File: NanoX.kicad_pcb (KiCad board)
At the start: 2 copper layers, 73.9 x 18.1 mm, 47 parts, among them J1 10118192-0001LF, J2 Conn_ARM_JTAG_SWD_10, J3 Conn_01x11, J4 NanoClassic_R, J5 Conn_01x11, J6 NanoClassic_L, SW1 SW_Push, U1 ATSAMD21G18A-AUT, U2 MCP1725-3302E_MC, U3 CAT24C16YI-GT3

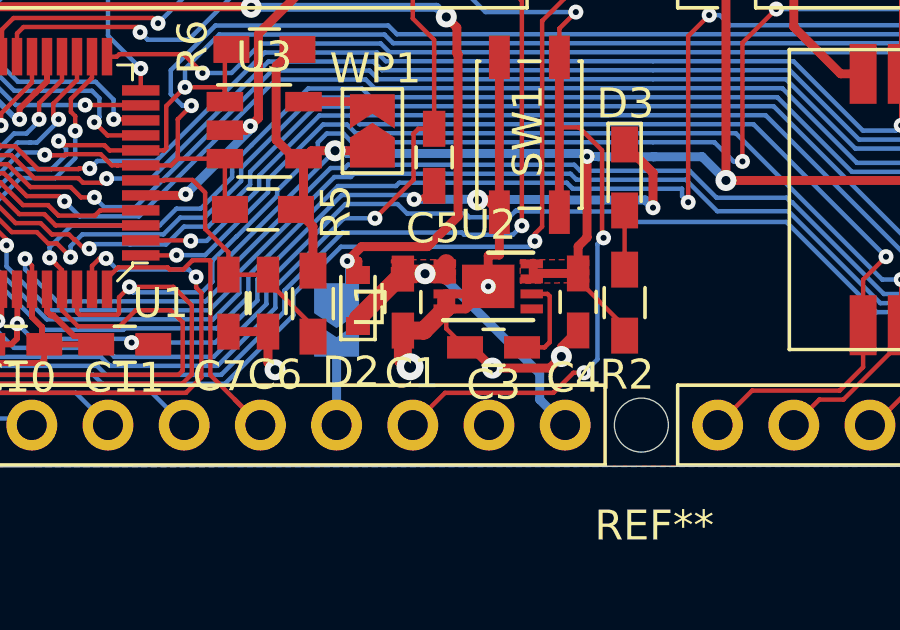
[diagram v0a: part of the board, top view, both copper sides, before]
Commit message: Change pin 3 of MCP1725 to Vin instead of GND.
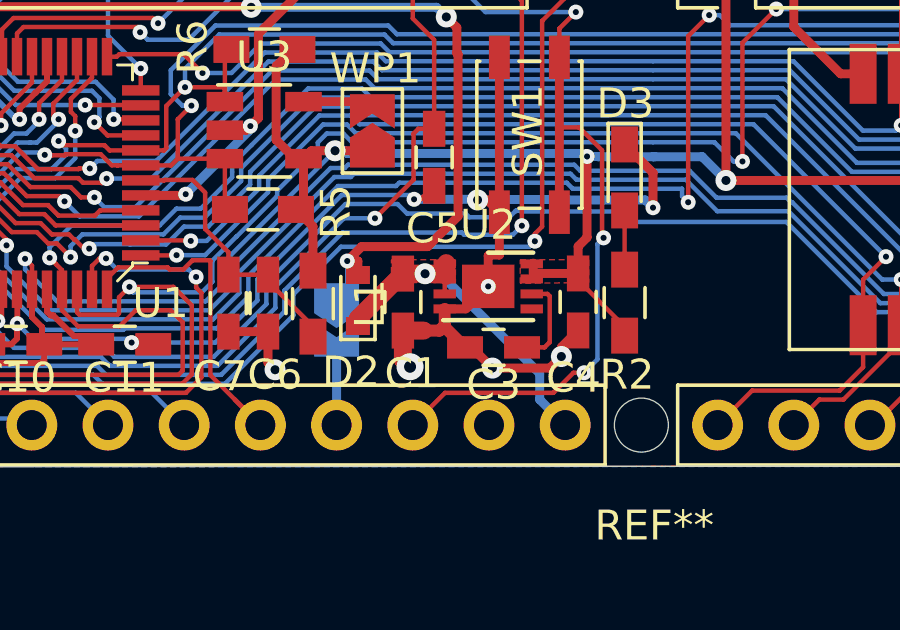
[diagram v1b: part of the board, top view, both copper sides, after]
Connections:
- U2 pad 3: GND -> VIN
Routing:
- net VIN: track 11.5 -> 12.0 mm
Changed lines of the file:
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@@
     (thickness 1.6)
     (drawings 60)
-    (tracks 1395)
+    (tracks 1398)
     (zones 0)
     (modules 47)
@@
   )
   (setup
-    (last_trace_width 0.15)
+    (last_trace_width 0.3)
     (user_trace_width 0.2)
     (user_trace_width 0.3)
@@
     (solder_mask_min_width 0.1016)
     (aux_axis_origin 0 0)
-    (visible_elements FFFFFF7F)
+    (visible_elements FFFFF77F)
     (pcbplotparams
       (layerselection 0x010f0_ffffffff)
@@
       (drillshape 0)
       (scaleselection 1)
-      (outputdirectory "Gerber-20200928/"))
+      (outputdirectory "Gerber-20201025"))
   )
   (net 0 "")
@@
       (effects (font (size 1 1) (thickness 0.15)))
     )
-    (fp_line (start 0 -1.125) (end 1.5 -1.125) (layer F.SilkS) (width 0.15))
-    (fp_line (start -1.5 1.125) (end 1.5 1.125) (layer F.SilkS) (width 0.15))
-    (fp_line (start -2.1 1.3) (end 2.1 1.3) (layer F.CrtYd) (width 0.05))
-    (fp_line (start -2.1 -1.3) (end 2.1 -1.3) (layer F.CrtYd) (width 0.05))
-    (fp_line (start 2.1 -1.3) (end 2.1 1.3) (layer F.CrtYd) (width 0.05))
-    (fp_line (start -2.1 -1.3) (end -2.1 1.3) (layer F.CrtYd) (width 0.05))
-    (fp_line (start -1.5 0) (end -0.5 -1) (layer F.Fab) (width 0.15))
-    (fp_line (start -1.5 1) (end -1.5 0) (layer F.Fab) (width 0.15))
-    (fp_line (start 1.5 1) (end -1.5 1) (layer F.Fab) (width 0.15))
-    (fp_line (start 1.5 -1) (end 1.5 1) (layer F.Fab) (width 0.15))
-    (fp_line (start -0.5 -1) (end 1.5 -1) (layer F.Fab) (width 0.15))
     (fp_text user %R (at 0 0) (layer F.Fab)
       (effects (font (size 0.7 0.7) (thickness 0.105)))
     )
-    (pad "" smd rect (at -0.4375 -0.3625) (size 0.71 0.58) (layers F.Paste))
-    (pad "" smd rect (at 0.4375 -0.3625) (size 0.71 0.58) (layers F.Paste))
-    (pad "" smd rect (at 0.4375 0.3625) (size 0.71 0.58) (layers F.Paste))
-    (pad 9 smd rect (at 0 0) (size 1.75 1.45) (layers F.Cu F.Mask)
-      (net 2 GND))
-    (pad "" smd rect (at -0.4375 0.3625) (size 0.71 0.58) (layers F.Paste))
+    (fp_line (start -0.5 -1) (end 1.5 -1) (layer F.Fab) (width 0.15))
+    (fp_line (start 1.5 -1) (end 1.5 1) (layer F.Fab) (width 0.15))
+    (fp_line (start 1.5 1) (end -1.5 1) (layer F.Fab) (width 0.15))
+    (fp_line (start -1.5 1) (end -1.5 0) (layer F.Fab) (width 0.15))
+    (fp_line (start -1.5 0) (end -0.5 -1) (layer F.Fab) (width 0.15))
+    (fp_line (start -2.1 -1.3) (end -2.1 1.3) (layer F.CrtYd) (width 0.05))
+    (fp_line (start 2.1 -1.3) (end 2.1 1.3) (layer F.CrtYd) (width 0.05))
+    (fp_line (start -2.1 -1.3) (end 2.1 -1.3) (layer F.CrtYd) (width 0.05))
+    (fp_line (start -2.1 1.3) (end 2.1 1.3) (layer F.CrtYd) (width 0.05))
+    (fp_line (start -1.5 1.125) (end 1.5 1.125) (layer F.SilkS) (width 0.15))
+    (fp_line (start 0 -1.125) (end 1.5 -1.125) (layer F.SilkS) (width 0.15))
+    (pad 1 smd rect (at -1.45 -0.75) (size 0.75 0.3) (layers F.Cu F.Paste F.Mask)
+      (net 1 VIN))
+    (pad 2 smd rect (at -1.45 -0.25) (size 0.75 0.3) (layers F.Cu F.Paste F.Mask)
+      (net 1 VIN))
+    (pad 3 smd rect (at -1.45 0.25) (size 0.75 0.3) (layers F.Cu F.Paste F.Mask)
+      (net 1 VIN))
+    (pad 4 smd rect (at -1.45 0.75) (size 0.75 0.3) (layers F.Cu F.Paste F.Mask)
+      (net 2 GND))
+    (pad 5 smd rect (at 1.45 0.75) (size 0.75 0.3) (layers F.Cu F.Paste F.Mask)
+      (net 48 "Net-(U2-Pad5)"))
+    (pad 6 smd rect (at 1.45 0.25) (size 0.75 0.3) (layers F.Cu F.Paste F.Mask)
+      (net 4 "Net-(C3-Pad1)"))
+    (pad 7 smd rect (at 1.45 -0.25) (size 0.75 0.3) (layers F.Cu F.Paste F.Mask)
+      (net 5 VDD))
     (pad 8 smd rect (at 1.45 -0.75) (size 0.75 0.3) (layers F.Cu F.Paste F.Mask)
       (net 5 VDD))
-    (pad 7 smd rect (at 1.45 -0.25) (size 0.75 0.3) (layers F.Cu F.Paste F.Mask)
-      (net 5 VDD))
-    (pad 6 smd rect (at 1.45 0.25) (size 0.75 0.3) (layers F.Cu F.Paste F.Mask)
-      (net 4 "Net-(C3-Pad1)"))
-    (pad 5 smd rect (at 1.45 0.75) (size 0.75 0.3) (layers F.Cu F.Paste F.Mask)
-      (net 48 "Net-(U2-Pad5)"))
-    (pad 4 smd rect (at -1.45 0.75) (size 0.75 0.3) (layers F.Cu F.Paste F.Mask)
-      (net 2 GND))
-    (pad 3 smd rect (at -1.45 0.25) (size 0.75 0.3) (layers F.Cu F.Paste F.Mask)
-      (net 2 GND))
-    (pad 2 smd rect (at -1.45 -0.25) (size 0.75 0.3) (layers F.Cu F.Paste F.Mask)
-      (net 1 VIN))
-    (pad 1 smd rect (at -1.45 -0.75) (size 0.75 0.3) (layers F.Cu F.Paste F.Mask)
-      (net 1 VIN))
+    (pad "" smd rect (at -0.4375 0.3625) (size 0.71 0.58) (layers F.Paste))
+    (pad 9 smd rect (at 0 0) (size 1.75 1.45) (layers F.Cu F.Mask)
+      (net 2 GND))
+    (pad "" smd rect (at 0.4375 0.3625) (size 0.71 0.58) (layers F.Paste))
+    (pad "" smd rect (at 0.4375 -0.3625) (size 0.71 0.58) (layers F.Paste))
+    (pad "" smd rect (at -0.4375 -0.3625) (size 0.71 0.58) (layers F.Paste))
     (model ${KISYS3DMOD}/Package_DFN_QFN.3dshapes/DFN-8-1EP_3x2mm_P0.5mm_EP1.75x1.45mm.wrl
       (at (xyz 0 0 0))
@@
   (gr_line (start 149.7076 102.616) (end 106.2736 102.6414) (layer Edge.Cuts) (width 0.05))
   (gr_line (start 106.299 84.6074) (end 149.7076 84.582) (layer Edge.Cuts) (width 0.05))
+  (via (at 143.2052 96.6216) (size 0.5) (drill 0.2) (layers F.Cu B.Cu) (net 2))
+  (segment (start 142.9552 96.8716) (end 143.2052 96.6216) (width 0.3) (layer F.Cu) (net 2))
+  (segment (start 143.4084 96.6216) (end 143.5768 96.4532) (width 0.3) (layer F.Cu) (net 2))
+  (segment (start 143.2052 96.6216) (end 143.4084 96.6216) (width 0.3) (layer F.Cu) (net 2))
   (segment (start 138.8618 97.6934) (end 140.3604 96.1948) (width 0.6) (layer F.Cu) (net 1) (status 30))
   (segment (start 138.8618 97.9424) (end 138.8618 97.6934) (width 0.6) (layer F.Cu) (net 1) (status 30))
@@
   (segment (start 141.594974 96.2) (end 144.920601 99.525627) (width 0.3) (layer B.Cu) (net 1))
   (segment (start 141.1 96.2) (end 141.594974 96.2) (width 0.3) (layer B.Cu) (net 1))
+  (segment (start 141.7552 96.8716) (end 141.7552 96.3716) (width 0.15) (layer F.Cu) (net 1))
   (via (at 111.633 94.9452) (size 0.5) (drill 0.2) (layers F.Cu B.Cu) (net 2))
   (segment (start 111.6284 94.9498) (end 111.633 94.9452) (width 0.3) (layer F.Cu) (net 2))
@@
   (segment (start 135.51005 96.389424) (end 138.323685 93.575789) (width 0.15) (layer B.Cu) (net 2))
   (segment (start 143.5768 88.987) (end 143.5768 94.147) (width 0.3) (layer F.Cu) (net 2) (status 30))
-  (segment (start 141.0574 98.0948) (end 141.806 97.3462) (width 0.6) (layer F.Cu) (net 2) (status 20))
   (segment (start 140.3604 98.0948) (end 141.0574 98.0948) (width 0.6) (layer F.Cu) (net 2) (status 10))
   (via (at 140.6 99.3) (size 0.9) (drill 0.4) (layers F.Cu B.Cu) (net 2))
@@
   (segment (start 145.6436 98.6486) (end 146.2024 98.0898) (width 0.3) (layer F.Cu) (net 2) (status 20))
   (segment (start 145.6436 98.9584) (end 145.6436 98.6486) (width 0.3) (layer F.Cu) (net 2))
-  (segment (start 141.806 97.3462) (end 141.806 97.021199) (width 0.6) (layer F.Cu) (net 2))
   (via (at 109.0168 99.0092) (size 0.5) (drill 0.2) (layers F.Cu B.Cu) (net 2))
   (via (at 119.0244 93.4212) (size 0.5) (drill 0.2) (layers F.Cu B.Cu) (net 2))
@@
   (segment (start 123.022799 95.786525) (end 123.022799 95.164601) (width 0.15) (layer F.Cu) (net 2))
   (segment (start 121.476524 97.3328) (end 123.022799 95.786525) (width 0.15) (layer F.Cu) (net 2))
-  (segment (start 143.2052 96.6216) (end 143.4084 96.6216) (width 0.3) (layer F.Cu) (net 2))
-  (segment (start 143.4084 96.6216) (end 143.5768 96.4532) (width 0.3) (layer F.Cu) (net 2))
-  (segment (start 142.9552 96.8716) (end 143.2052 96.6216) (width 0.3) (layer F.Cu) (net 2))
-  (segment (start 141.7552 96.8716) (end 142.9552 96.8716) (width 0.3) (layer F.Cu) (net 2))
+  (segment (start 143.5768 95.5754) (end 143.2264 95.5754) (width 0.3) (layer F.Cu) (net 2))
+  (segment (start 143.2264 95.5754) (end 143.2052 95.5966) (width 0.3) (layer F.Cu) (net 2))
+  (segment (start 143.2052 95.5966) (end 143.2052 96.6216) (width 0.3) (layer F.Cu) (net 2))
   (segment (start 142.4552 97.3716) (end 143.2052 96.6216) (width 0.3) (layer F.Cu) (net 2))
+  (segment (start 141.7552 97.9216) (end 141.7552 97.3716) (width 0.4) (layer F.Cu) (net 2))
+  (segment (start 141.582 98.0948) (end 141.7552 97.9216) (width 0.4) (layer F.Cu) (net 2))
+  (segment (start 141.0574 98.0948) (end 141.582 98.0948) (width 0.4) (layer F.Cu) (net 2))
+  (segment (start 141.7552 97.9758) (end 142.433 98.6536) (width 0.4) (layer F.Cu) (net 2))
+  (segment (start 141.7552 97.9216) (end 141.7552 97.9758) (width 0.4) (layer F.Cu) (net 2))
   (segment (start 141.7552 97.3716) (end 142.4552 97.3716) (width 0.3) (layer F.Cu) (net 2))
-  (segment (start 143.2052 95.5966) (end 143.2052 96.6216) (width 0.3) (layer F.Cu) (net 2))
-  (via (at 143.2052 96.6216) (size 0.5) (drill 0.2) (layers F.Cu B.Cu) (net 2))
-  (segment (start 143.2264 95.5754) (end 143.2052 95.5966) (width 0.3) (layer F.Cu) (net 2))
-  (segment (start 143.5768 95.5754) (end 143.2264 95.5754) (width 0.3) (layer F.Cu) (net 2))
   (segment (start 109.673 89.8498) (end 110.373 90.5498) (width 0.25) (layer F.Cu) (net 3) (status 30))
   (segment (start 107.823 89.8498) (end 109.673 89.8498) (width 0.25) (layer F.Cu) (net 3) (status 30))

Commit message: Bump revision to P2.
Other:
- board text added: "NanoX Rev. P2 https://github.com/Bu-Gee/NanoX Copyright(c) 2020, Fortian Inc. Licensed Under CC-BY-NC-SA 3.0"
- board text removed: "NanoX Rev. P1 https://github.com/Bu-Gee/NanoX Copyright(c) 2020, Fortian Inc. Licensed Under CC-BY-NC-SA 3.0"
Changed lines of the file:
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@@
   )
   (setup
-    (last_trace_width 0.3)
+    (last_trace_width 0.15)
     (user_trace_width 0.2)
     (user_trace_width 0.3)
@@
     (effects (font (size 0.8 0.8) (thickness 0.15)))
   )
-  (gr_text "NanoX   Rev. P1\nhttps://github.com/Bu-Gee/NanoX\nCopyright(c) 2020, Fortian Inc.\nLicensed Under CC-BY-NC-SA 3.0\n" (at 136.398 91.694) (layer B.SilkS)
+  (gr_text "NanoX   Rev. P2\nhttps://github.com/Bu-Gee/NanoX\nCopyright(c) 2020, Fortian Inc.\nLicensed Under CC-BY-NC-SA 3.0\n" (at 136.398 91.694) (layer B.SilkS)
     (effects (font (size 0.8 0.8) (thickness 0.15)) (justify mirror))
   )
@@
   (gr_line (start 149.7076 102.616) (end 106.2736 102.6414) (layer Edge.Cuts) (width 0.05))
   (gr_line (start 106.299 84.6074) (end 149.7076 84.582) (layer Edge.Cuts) (width 0.05))
-  (via (at 143.2052 96.6216) (size 0.5) (drill 0.2) (layers F.Cu B.Cu) (net 2))
-  (segment (start 142.9552 96.8716) (end 143.2052 96.6216) (width 0.3) (layer F.Cu) (net 2))
-  (segment (start 143.4084 96.6216) (end 143.5768 96.4532) (width 0.3) (layer F.Cu) (net 2))
-  (segment (start 143.2052 96.6216) (end 143.4084 96.6216) (width 0.3) (layer F.Cu) (net 2))
   (segment (start 138.8618 97.6934) (end 140.3604 96.1948) (width 0.6) (layer F.Cu) (net 1) (status 30))
   (segment (start 138.8618 97.9424) (end 138.8618 97.6934) (width 0.6) (layer F.Cu) (net 1) (status 30))
@@
   (segment (start 141.1 96.2) (end 141.594974 96.2) (width 0.3) (layer B.Cu) (net 1))
   (segment (start 141.7552 96.8716) (end 141.7552 96.3716) (width 0.15) (layer F.Cu) (net 1))
+  (via (at 143.2052 96.6216) (size 0.5) (drill 0.2) (layers F.Cu B.Cu) (net 2))
+  (segment (start 142.9552 96.8716) (end 143.2052 96.6216) (width 0.3) (layer F.Cu) (net 2))
+  (segment (start 143.4084 96.6216) (end 143.5768 96.4532) (width 0.3) (layer F.Cu) (net 2))
+  (segment (start 143.2052 96.6216) (end 143.4084 96.6216) (width 0.3) (layer F.Cu) (net 2))
   (via (at 111.633 94.9452) (size 0.5) (drill 0.2) (layers F.Cu B.Cu) (net 2))
   (segment (start 111.6284 94.9498) (end 111.633 94.9452) (width 0.3) (layer F.Cu) (net 2))
